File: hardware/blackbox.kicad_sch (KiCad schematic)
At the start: 0 parts

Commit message: wip: schematic sheets in progress
Co-Authored-By: Claude Opus 5.5 <noreply@anthropic.com>
Claude-Session: https://claude.ai/code/session_01RFaS5jnC9tnPam9GBgmGnG
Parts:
- added C65: 100nF, lib:C_0201_0603Metric_W, symbol Device:C
- added R50: 10k, lib:R_0201_0603Metric_W, symbol Device:R
- added U13: PY25Q128HA-DFH-IR, lib:USON-8_3x3mm_P0.8mm_EP_PY25Q128HA, symbol lib:PY25Q128HA-DFH-IR
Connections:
- new net +3V3: C65.1, R50.1, U13.3 (~{WP}/IO2), U13.7 (~{HOLD}/~{RESET}/IO3), U13.8 (VCC)
- new net FLASH_CS: R50.2, U13.1 (~{CS})
- new net GND: C65.2, U13.4 (GND)
- new net SPI0_MISO: U13.2 (SO/IO1)
- new net SPI0_MOSI: U13.5 (SI/IO0)
- new net SPI0_SCK: U13.6 (SCLK)
- no-connect marks 0 -> 1
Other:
- note added: "SPI NOR PY25Q128HA: 16 MB blackbox on SPI0 (U13 C65 R50)"

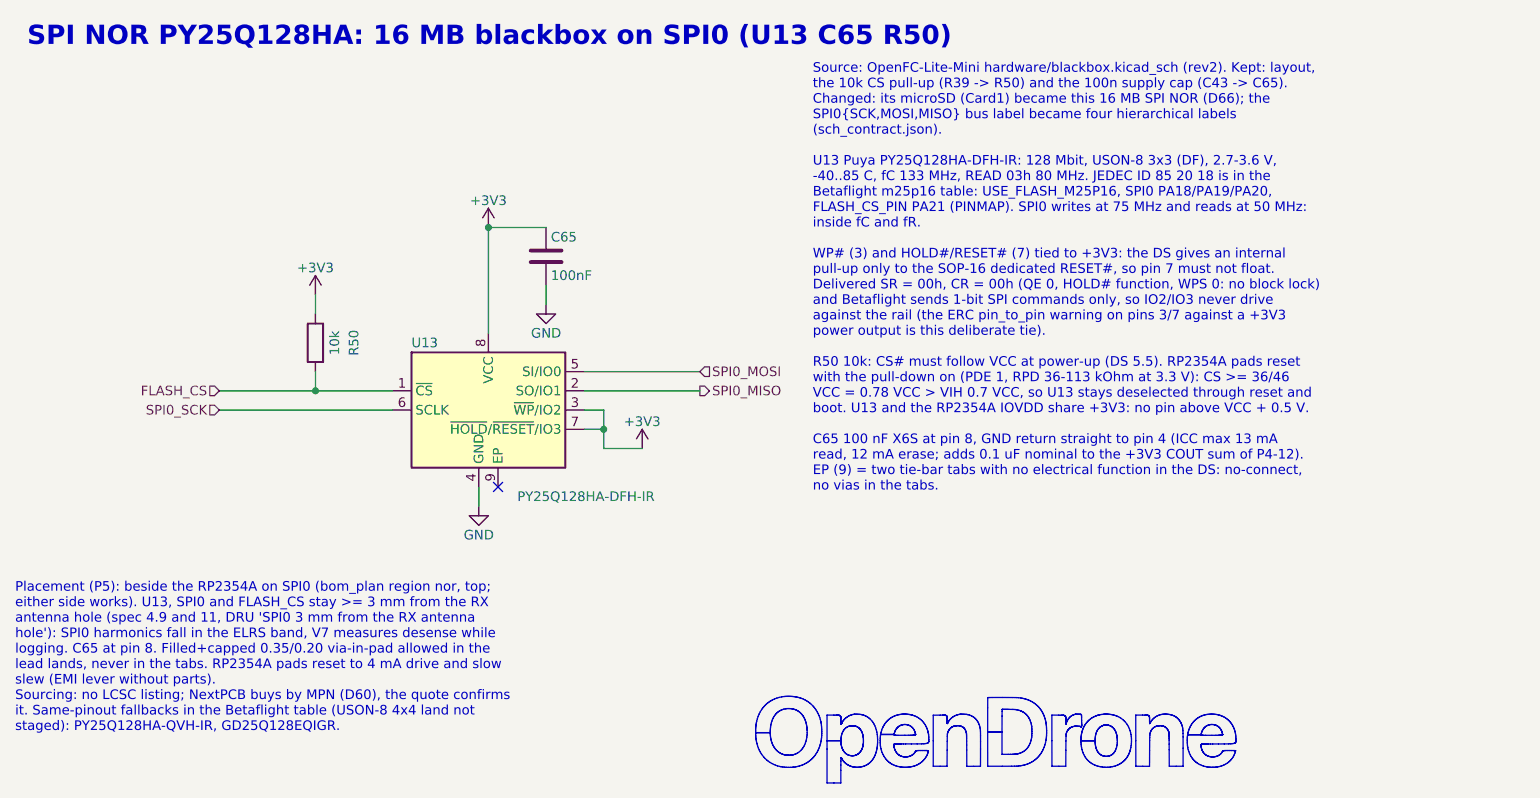
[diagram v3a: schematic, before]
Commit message: hardware: floorplan v3 review pass (RX RF corner blocker fixed; majors listed in FLOORPLAN.md Open)
Co-Authored-By: Claude Opus 5.5 <noreply@anthropic.com>
Claude-Session: https://claude.ai/code/session_01RFaS5jnC9tnPam9GBgmGnG
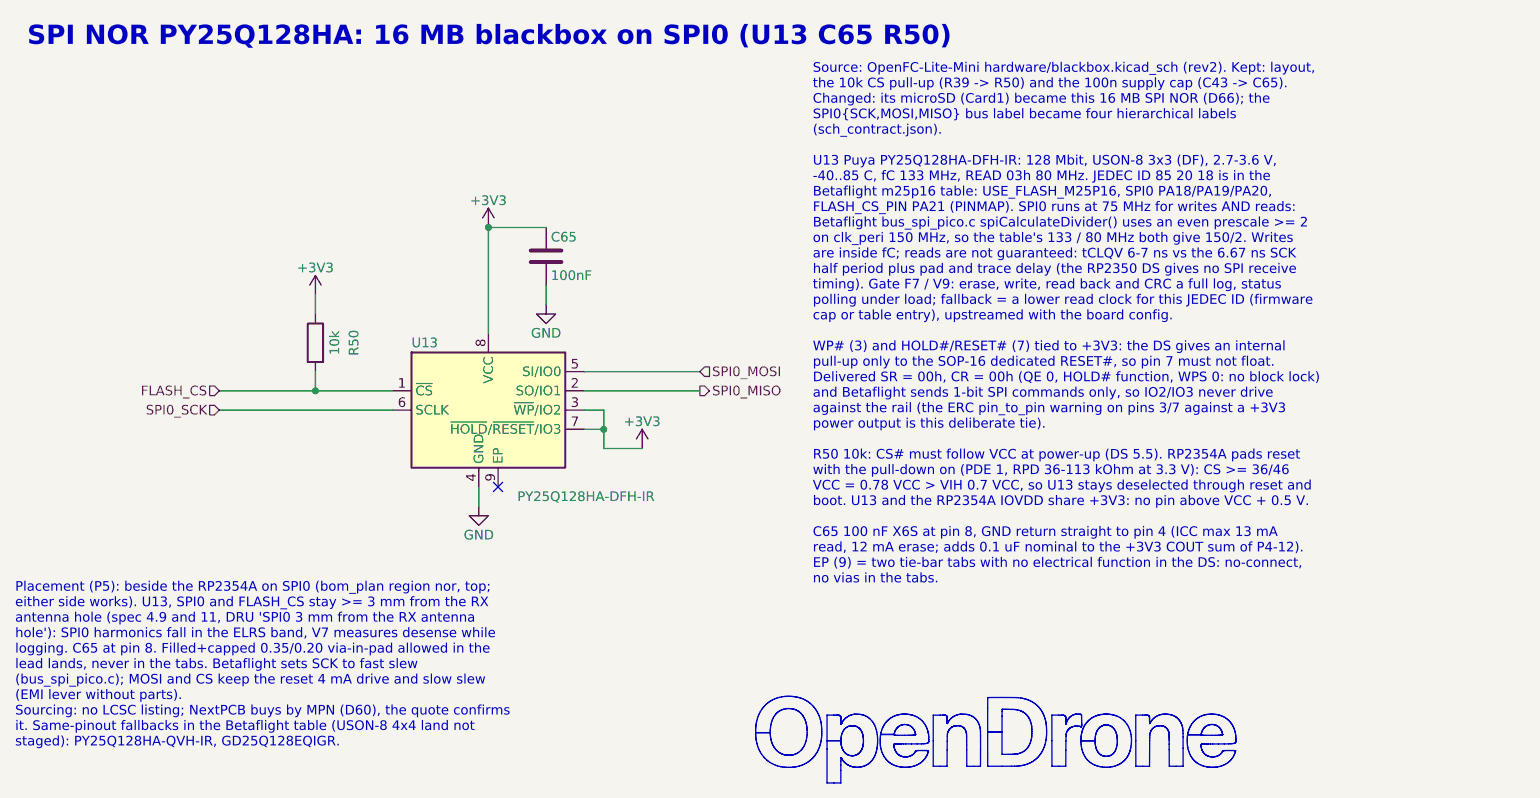
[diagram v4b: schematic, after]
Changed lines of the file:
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@@
 		)
 	)
-	(text_box "Placement (P5): beside the RP2354A on SPI0 (bom_plan region nor, top; either side works). U13, SPI0 and FLASH_CS stay >= 3 mm from the RX antenna hole (spec 4.9 and 11, DRU 'SPI0 3 mm from the RX antenna hole'): SPI0 harmonics fall in the ELRS band, V7 measures desense while logging. C65 at pin 8. Filled+capped 0.35/0.20 via-in-pad allowed in the lead lands, never in the tabs. RP2354A pads reset to 4 mA drive and slow slew (EMI lever without parts).\nSourcing: no LCSC listing; NextPCB buys by MPN (D60), the quote confirms it. Same-pinout fallbacks in the Betaflight table (USON-8 4x4 land not staged): PY25Q128HA-QVH-IR, GD25Q128EQIGR."
+	(text_box "Placement (P5): beside the RP2354A on SPI0 (bom_plan region nor, top; either side works). U13, SPI0 and FLASH_CS stay >= 3 mm from the RX antenna hole (spec 4.9 and 11, DRU 'SPI0 3 mm from the RX antenna hole'): SPI0 harmonics fall in the ELRS band, V7 measures desense while logging. C65 at pin 8. Filled+capped 0.35/0.20 via-in-pad allowed in the lead lands, never in the tabs. Betaflight sets SCK to fast slew (bus_spi_pico.c); MOSI and CS keep the reset 4 mA drive and slow slew (EMI lever without parts).\nSourcing: no LCSC listing; NextPCB buys by MPN (D60), the quote confirms it. Same-pinout fallbacks in the Betaflight table (USON-8 4x4 land not staged): PY25Q128HA-QVH-IR, GD25Q128EQIGR."
 		(exclude_from_sim no)
 		(at 12.7 90.17 0)
@@
 		)
 	)
-	(text_box "Source: OpenFC-Lite-Mini hardware/blackbox.kicad_sch (rev2). Kept: layout, the 10k CS pull-up (R39 -> R50) and the 100n supply cap (C43 -> C65). Changed: its microSD (Card1) became this 16 MB SPI NOR (D66); the SPI0{SCK,MOSI,MISO} bus label became four hierarchical labels (sch_contract.json).\n\nU13 Puya PY25Q128HA-DFH-IR: 128 Mbit, USON-8 3x3 (DF), 2.7-3.6 V, -40..85 C, fC 133 MHz, READ 03h 80 MHz. JEDEC ID 85 20 18 is in the Betaflight m25p16 table: USE_FLASH_M25P16, SPI0 PA18/PA19/PA20, FLASH_CS_PIN PA21 (PINMAP). SPI0 writes at 75 MHz and reads at 50 MHz: inside fC and fR.\n\nWP# (3) and HOLD#/RESET# (7) tied to +3V3: the DS gives an internal pull-up only to the SOP-16 dedicated RESET#, so pin 7 must not float. Delivered SR = 00h, CR = 00h (QE 0, HOLD# function, WPS 0: no block lock) and Betaflight sends 1-bit SPI commands only, so IO2/IO3 never drive against the rail (the ERC pin_to_pin warning on pins 3/7 against a +3V3 power output is this deliberate tie).\n\nR50 10k: CS# must follow VCC at power-up (DS 5.5). RP2354A pads reset with the pull-down on (PDE 1, RPD 36-113 kOhm at 3.3 V): CS >= 36/46 VCC = 0.78 VCC > VIH 0.7 VCC, so U13 stays deselected through reset and boot. U13 and the RP2354A IOVDD share +3V3: no pin above VCC + 0.5 V.\n\nC65 100 nF X6S at pin 8, GND return straight to pin 4 (ICC max 13 mA read, 12 mA erase; adds 0.1 uF nominal to the +3V3 COUT sum of P4-12). EP (9) = two tie-bar tabs with no electrical function in the DS: no-connect, no vias in the tabs."
+	(text_box "Source: OpenFC-Lite-Mini hardware/blackbox.kicad_sch (rev2). Kept: layout, the 10k CS pull-up (R39 -> R50) and the 100n supply cap (C43 -> C65). Changed: its microSD (Card1) became this 16 MB SPI NOR (D66); the SPI0{SCK,MOSI,MISO} bus label became four hierarchical labels (sch_contract.json).\n\nU13 Puya PY25Q128HA-DFH-IR: 128 Mbit, USON-8 3x3 (DF), 2.7-3.6 V, -40..85 C, fC 133 MHz, READ 03h 80 MHz. JEDEC ID 85 20 18 is in the Betaflight m25p16 table: USE_FLASH_M25P16, SPI0 PA18/PA19/PA20, FLASH_CS_PIN PA21 (PINMAP). SPI0 runs at 75 MHz for writes AND reads: Betaflight bus_spi_pico.c spiCalculateDivider() uses an even prescale >= 2 on clk_peri 150 MHz, so the table's 133 / 80 MHz both give 150/2. Writes are inside fC; reads are not guaranteed: tCLQV 6-7 ns vs the 6.67 ns SCK half period plus pad and trace delay (the RP2350 DS gives no SPI receive timing). Gate F7 / V9: erase, write, read back and CRC a full log, status polling under load; fallback = a lower read clock for this JEDEC ID (firmware cap or table entry), upstreamed with the board config.\n\nWP# (3) and HOLD#/RESET# (7) tied to +3V3: the DS gives an internal pull-up only to the SOP-16 dedicated RESET#, so pin 7 must not float. Delivered SR = 00h, CR = 00h (QE 0, HOLD# function, WPS 0: no block lock) and Betaflight sends 1-bit SPI commands only, so IO2/IO3 never drive against the rail (the ERC pin_to_pin warning on pins 3/7 against a +3V3 power output is this deliberate tie).\n\nR50 10k: CS# must follow VCC at power-up (DS 5.5). RP2354A pads reset with the pull-down on (PDE 1, RPD 36-113 kOhm at 3.3 V): CS >= 36/46 VCC = 0.78 VCC > VIH 0.7 VCC, so U13 stays deselected through reset and boot. U13 and the RP2354A IOVDD share +3V3: no pin above VCC + 0.5 V.\n\nC65 100 nF X6S at pin 8, GND return straight to pin 4 (ICC max 13 mA read, 12 mA erase; adds 0.1 uF nominal to the +3V3 COUT sum of P4-12). EP (9) = two tie-bar tabs with no electrical function in the DS: no-connect, no vias in the tabs."
 		(exclude_from_sim no)
 		(at 118.11 21.59 0)

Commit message: WIP final schematic (D111/D113): GPIO map, D100 oscillator, final footprints, lineup power-net names; mid-run snapshot, not yet verified (ERC/netlist/DRU regen pending)
Co-Authored-By: Claude Opus 5.5 <noreply@anthropic.com>
Claude-Session: https://claude.ai/code/session_01RFaS5jnC9tnPam9GBgmGnG
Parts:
- C65: footprint lib:C_0201_0603Metric_W -> lib:C_0201_0603Metric_L
- R50: footprint lib:R_0201_0603Metric_W -> lib:R_0201_0603Metric_L
- U13: footprint lib:USON-8_3x3mm_P0.8mm_EP_PY25Q128HA -> lib:USON-8_3x3mm_P0.8mm_EP_PY25Q128HA_L
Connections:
- net +3V3 renamed +3.3V
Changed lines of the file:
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@@
 		)
 	)
-	(text_box "Source: OpenFC-Lite-Mini hardware/blackbox.kicad_sch (rev2). Kept: layout, the 10k CS pull-up (R39 -> R50) and the 100n supply cap (C43 -> C65). Changed: its microSD (Card1) became this 16 MB SPI NOR (D66); the SPI0{SCK,MOSI,MISO} bus label became four hierarchical labels (sch_contract.json).\n\nU13 Puya PY25Q128HA-DFH-IR: 128 Mbit, USON-8 3x3 (DF), 2.7-3.6 V, -40..85 C, fC 133 MHz, READ 03h 80 MHz. JEDEC ID 85 20 18 is in the Betaflight m25p16 table: USE_FLASH_M25P16, SPI0 PA18/PA19/PA20, FLASH_CS_PIN PA21 (PINMAP). SPI0 runs at 75 MHz for writes AND reads: Betaflight bus_spi_pico.c spiCalculateDivider() uses an even prescale >= 2 on clk_peri 150 MHz, so the table's 133 / 80 MHz both give 150/2. Writes are inside fC; reads are not guaranteed: tCLQV 6-7 ns vs the 6.67 ns SCK half period plus pad and trace delay (the RP2350 DS gives no SPI receive timing). Gate F7 / V9: erase, write, read back and CRC a full log, status polling under load; fallback = a lower read clock for this JEDEC ID (firmware cap or table entry), upstreamed with the board config.\n\nWP# (3) and HOLD#/RESET# (7) tied to +3V3: the DS gives an internal pull-up only to the SOP-16 dedicated RESET#, so pin 7 must not float. Delivered SR = 00h, CR = 00h (QE 0, HOLD# function, WPS 0: no block lock) and Betaflight sends 1-bit SPI commands only, so IO2/IO3 never drive against the rail (the ERC pin_to_pin warning on pins 3/7 against a +3V3 power output is this deliberate tie).\n\nR50 10k: CS# must follow VCC at power-up (DS 5.5). RP2354A pads reset with the pull-down on (PDE 1, RPD 36-113 kOhm at 3.3 V): CS >= 36/46 VCC = 0.78 VCC > VIH 0.7 VCC, so U13 stays deselected through reset and boot. U13 and the RP2354A IOVDD share +3V3: no pin above VCC + 0.5 V.\n\nC65 100 nF X6S at pin 8, GND return straight to pin 4 (ICC max 13 mA read, 12 mA erase; adds 0.1 uF nominal to the +3V3 COUT sum of P4-12). EP (9) = two tie-bar tabs with no electrical function in the DS: no-connect, no vias in the tabs."
+	(text_box "Source: OpenFC-Lite-Mini hardware/blackbox.kicad_sch (rev2). Kept: layout, the 10k CS pull-up (R39 -> R50) and the 100n supply cap (C43 -> C65). Changed: its microSD (Card1) became this 16 MB SPI NOR (D66); the SPI0{SCK,MOSI,MISO} bus label became four hierarchical labels (sch_contract.json).\n\nU13 Puya PY25Q128HA-DFH-IR: 128 Mbit, USON-8 3x3 (DF), 2.7-3.6 V, -40..85 C, fC 133 MHz, READ 03h 80 MHz. JEDEC ID 85 20 18 is in the Betaflight m25p16 table: USE_FLASH_M25P16, SPI0 PA18/PA19/PA20, FLASH_CS_PIN PA21 (PINMAP). SPI0 runs at 75 MHz for writes AND reads: Betaflight bus_spi_pico.c spiCalculateDivider() uses an even prescale >= 2 on clk_peri 150 MHz, so the table's 133 / 80 MHz both give 150/2. Writes are inside fC; reads are not guaranteed: tCLQV 6-7 ns vs the 6.67 ns SCK half period plus pad and trace delay (the RP2350 DS gives no SPI receive timing). Gate F7 / V9: erase, write, read back and CRC a full log, status polling under load; fallback = a lower read clock for this JEDEC ID (firmware cap or table entry), upstreamed with the board config.\n\nWP# (3) and HOLD#/RESET# (7) tied to +3.3V: the DS gives an internal pull-up only to the SOP-16 dedicated RESET#, so pin 7 must not float. Delivered SR = 00h, CR = 00h (QE 0, HOLD# function, WPS 0: no block lock) and Betaflight sends 1-bit SPI commands only, so IO2/IO3 never drive against the rail (the ERC pin_to_pin warning on pins 3/7 against a +3.3V power output is this deliberate tie).\n\nR50 10k: CS# must follow VCC at power-up (DS 5.5). RP2354A pads reset with the pull-down on (PDE 1, RPD 36-113 kOhm at 3.3 V): CS >= 36/46 VCC = 0.78 VCC > VIH 0.7 VCC, so U13 stays deselected through reset and boot. U13 and the RP2354A IOVDD share +3.3V: no pin above VCC + 0.5 V.\n\nC65 100 nF X6S at pin 8, GND return straight to pin 4 (ICC max 13 mA read, 12 mA erase; adds 0.1 uF nominal to the +3.3V COUT sum of P4-12). EP (9) = two tie-bar tabs with no electrical function in the DS: no-connect, no vias in the tabs."
 		(exclude_from_sim no)
 		(at 118.11 21.59 0)
@@
 	)
 	(symbol
-		(lib_id "power:+3V3")
+		(lib_id "power:+3.3V")
 		(at 96.52 73.66 0)
 		(unit 1)
@@
 		(in_pos_files no)
 		(dnp no)
-		(property "Reference" "#PWR144"
+		(property "Reference" "#PWR145"
 			(at 96.52 77.47 0)
 			(hide yes)
@@
 			)
 		)
-		(property "Value" "+3V3"
+		(property "Value" "+3.3V"
 			(at 96.52 70.104 0)
 			(show_name no)
@@
 			)
 		)
-		(property "Description" "Power symbol creates a global label with name \"+3V3\""
+		(property "Description" "Power symbol creates a global label with name \"+3.3V\""
 			(at 96.52 73.66 0)
 			(hide yes)
@@
 			(project "OpenAIO-Whoop"
 				(path "/2c3a7206-1e66-4d43-a02f-491225e20dd6/04f14c5a-8e46-5d66-be84-2bb8762684a3"
-					(reference "#PWR144")
+					(reference "#PWR145")
 					(unit 1)
 				)
@@
 		(in_pos_files no)
 		(dnp no)
-		(property "Reference" "#PWR143"
+		(property "Reference" "#PWR144"
 			(at 83.82 60.96 0)
 			(hide yes)
@@
 			(project "OpenAIO-Whoop"
 				(path "/2c3a7206-1e66-4d43-a02f-491225e20dd6/04f14c5a-8e46-5d66-be84-2bb8762684a3"
-					(reference "#PWR143")
+					(reference "#PWR144")
 					(unit 1)
 				)
@@
 	)
 	(symbol
-		(lib_id "power:+3V3")
+		(lib_id "power:+3.3V")
 		(at 53.34 53.34 0)
 		(unit 1)
@@
 		(in_pos_files no)
 		(dnp no)
-		(property "Reference" "#PWR142"
+		(property "Reference" "#PWR143"
 			(at 53.34 57.15 0)
 			(hide yes)
@@
 			)
 		)
-		(property "Value" "+3V3"
+		(property "Value" "+3.3V"
 			(at 53.34 49.784 0)
 			(show_name no)
@@
 			)
 		)
-		(property "Description" "Power symbol creates a global label with name \"+3V3\""
+		(property "Description" "Power symbol creates a global label with name \"+3.3V\""
 			(at 53.34 53.34 0)
 			(hide yes)
@@
 			(project "OpenAIO-Whoop"
 				(path "/2c3a7206-1e66-4d43-a02f-491225e20dd6/04f14c5a-8e46-5d66-be84-2bb8762684a3"
-					(reference "#PWR142")
+					(reference "#PWR143")
 					(unit 1)
 				)
@@
 			)
 		)
-		(property "Footprint" "lib:C_0201_0603Metric_W"
+		(property "Footprint" "lib:C_0201_0603Metric_L"
 			(at 83.82 48.26 0)
 			(hide yes)
@@
 		(in_pos_files no)
 		(dnp no)
-		(property "Reference" "#PWR145"
+		(property "Reference" "#PWR146"
 			(at 74.93 87.63 0)
 			(hide yes)
@@
 			(project "OpenAIO-Whoop"
 				(path "/2c3a7206-1e66-4d43-a02f-491225e20dd6/04f14c5a-8e46-5d66-be84-2bb8762684a3"
-					(reference "#PWR145")
+					(reference "#PWR146")
 					(unit 1)
 				)
@@
 	)
 	(symbol
-		(lib_id "power:+3V3")
+		(lib_id "power:+3.3V")
 		(at 76.2 44.45 0)
 		(unit 1)
@@
 		(in_pos_files no)
 		(dnp no)
-		(property "Reference" "#PWR141"
+		(property "Reference" "#PWR142"
 			(at 76.2 48.26 0)
 			(hide yes)
@@
 			)
 		)
-		(property "Value" "+3V3"
+		(property "Value" "+3.3V"
 			(at 76.2 40.894 0)
 			(show_name no)
@@
 			)
 		)
-		(property "Description" "Power symbol creates a global label with name \"+3V3\""
+		(property "Description" "Power symbol creates a global label with name \"+3.3V\""
 			(at 76.2 44.45 0)
 			(hide yes)
@@
 			(project "OpenAIO-Whoop"
 				(path "/2c3a7206-1e66-4d43-a02f-491225e20dd6/04f14c5a-8e46-5d66-be84-2bb8762684a3"
-					(reference "#PWR141")
+					(reference "#PWR142")
 					(unit 1)
 				)
@@
 			)
 		)
-		(property "Footprint" "lib:R_0201_0603Metric_W"
+		(property "Footprint" "lib:R_0201_0603Metric_L"
 			(at 53.34 59.69 0)
 			(hide yes)
@@
 			)
 		)
-		(property "Footprint" "lib:USON-8_3x3mm_P0.8mm_EP_PY25Q128HA"
+		(property "Footprint" "lib:USON-8_3x3mm_P0.8mm_EP_PY25Q128HA_L"
 			(at 76.2 68.58 0)
 			(hide yes)
